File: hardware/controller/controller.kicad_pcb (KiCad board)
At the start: 4 copper layers, 53.8 x 35 mm, 82 parts, among them J1 Bus_PCI_Express_x1, J2 USB, J4 BM03B-SRSS-TB(LF)(SN), J6 RJ45_Hanrun_HR913550A_Horizon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, SW1 434133025816, SW2 434133025816, U1 RP2350A, U2 NCP1117ST33T3G, U3 W25Q128JVSIQ, U4 W6100-L, U5 RPi Radio Module 2, X1 12MHz, Y2 X322525MRB4SI

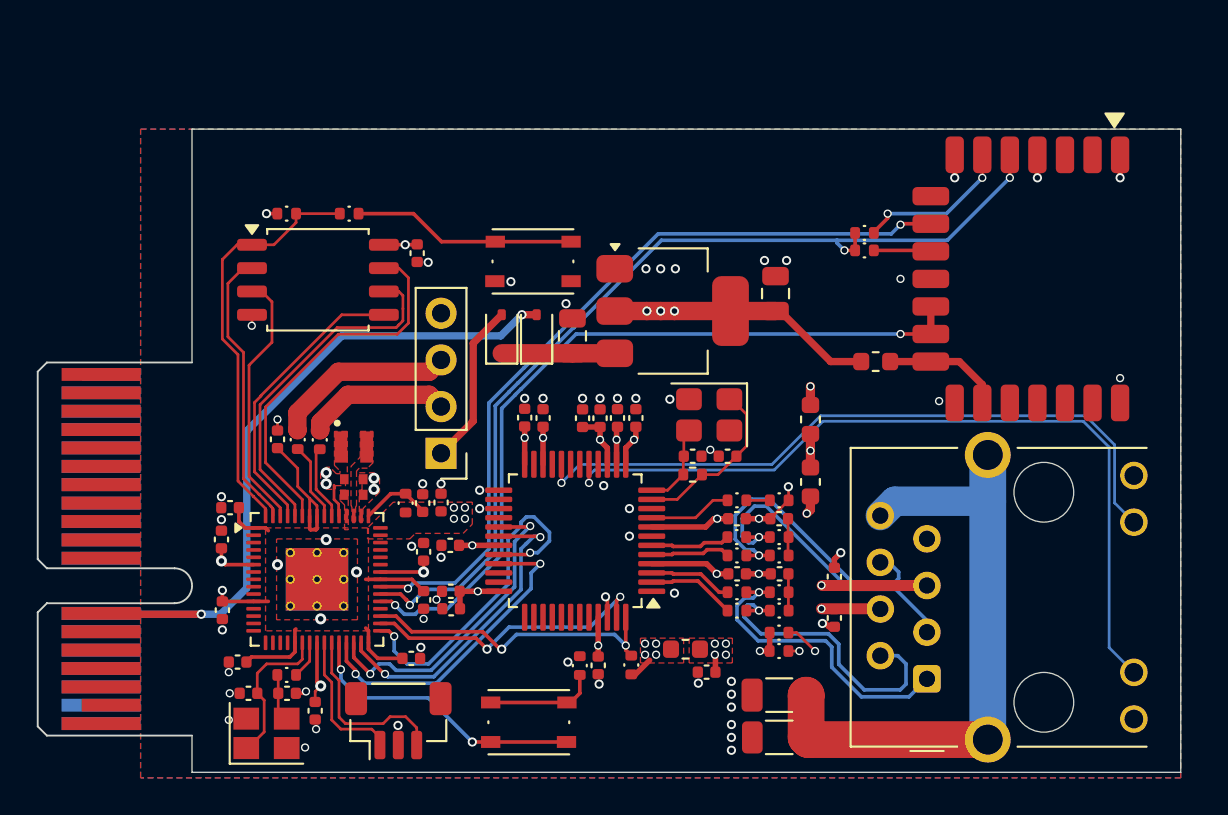
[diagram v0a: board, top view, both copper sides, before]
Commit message: feat(controller): add RPi RM2 and wire up remaining pins
fix(controller): move rj45 jack inset 1mm
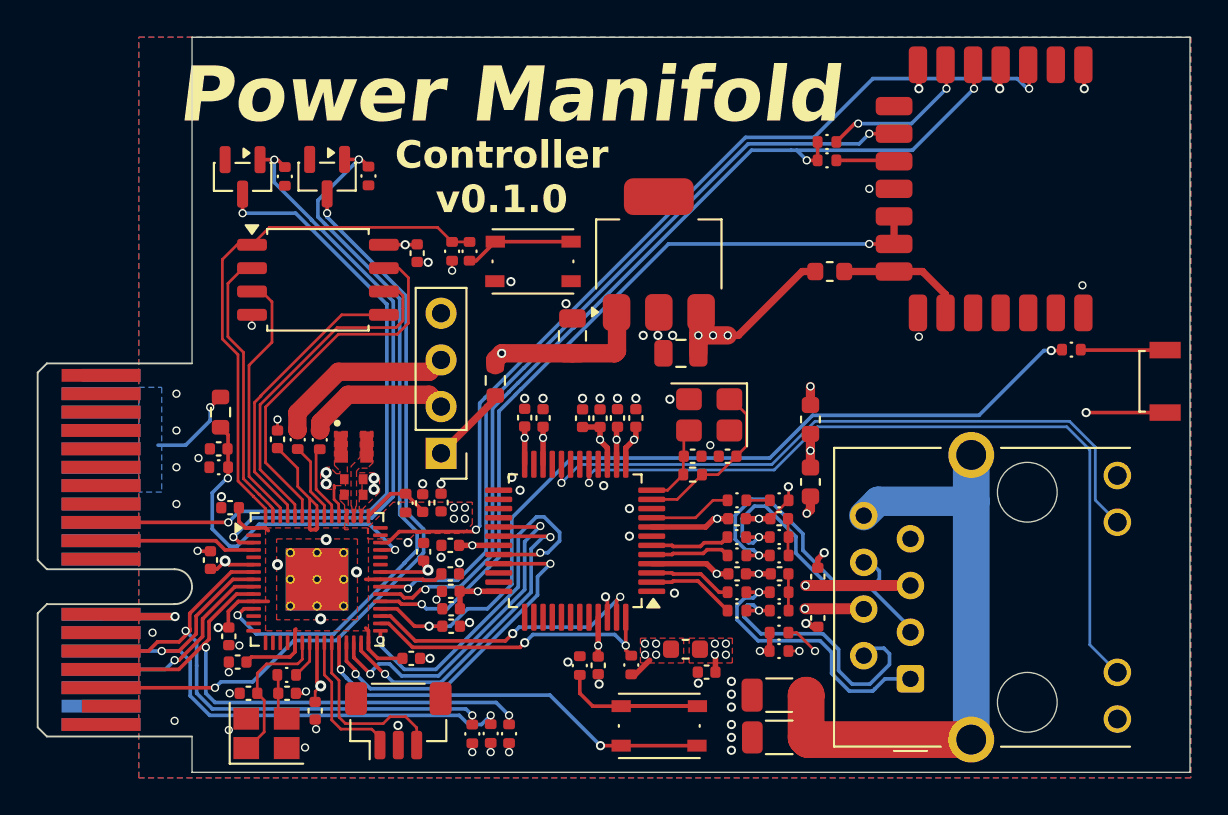
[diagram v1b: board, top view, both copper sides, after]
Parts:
- removed D1, D2: 1N5819WS, Diode_SMD:D_SOD-323
- added C18: 100nF, Capacitor_SMD:C_0402_1005Metric, F.Cu at (64.5, 57.4)
- added C27: 100nF, Capacitor_SMD:C_0402_1005Metric, F.Cu at (77.2, 67.0)
- added Q1: 2N7002, Package_TO_SOT_SMD:SOT-23, F.Cu at (65.8, 42.6)
- added Q2: 2N7002, Package_TO_SOT_SMD:SOT-23, F.Cu at (70.4, 42.6)
- added R10: 100K, Local Library:R_0402_1005Metric, F.Cu at (68.1, 42.6)
- added R11: 100K, Local Library:R_0402_1005Metric, F.Cu at (72.7, 42.5)
- added R12: 0R, Local Library:R_0603_1608Metric, F.Cu at (79.5, 53.7)
- added R13: 120K, Local Library:R_0603_1608Metric, F.Cu at (64.6, 55.4)
- added R14: 10K, Local Library:R_0402_1005Metric, F.Cu at (64.5, 58.4)
- added R15: 1K, Local Library:R_0402_1005Metric, F.Cu at (110.9, 52.0)
- added R32: 4.7K, Local Library:R_0402_1005Metric, F.Cu at (78.3, 72.9)
- added R41: 4.7K, Local Library:R_0402_1005Metric, F.Cu at (79.3, 72.9)
- added R43: 4.7K, Local Library:R_0402_1005Metric, F.Cu at (80.3, 72.9)
- added SW3: SW_Push, Button_Switch_SMD:SW_SPST_B3U-3000P, F.Cu at (116.0, 53.7)
- U2: value NCP1117ST33T3G -> AP7361C-33E; footprint Package_TO_SOT_SMD:SOT-223 -> Package_TO_SOT_SMD:SOT-223-3_TabPin2
- moved R1 9.23 mm to (77.2, 46.6), turned to 90 degrees
- moved SW2 7.10 mm to (88.5, 72.5)
- moved R6 6.86 mm to (78.2, 46.6), turned to -90 degrees
- moved C5 6.09 mm to (89.7, 52.2), turned to 180 degrees
- moved FB4 5.50 mm to (97.8, 47.8)
- moved R5 5.35 mm to (97.6, 40.7)
- moved R9 5.31 mm to (97.6, 41.7)
- moved U5 5.29 mm to (109.0, 43.2)
- moved U2 3.17 mm to (88.5, 46.8), turned to 90 degrees
- moved C13 2.03 mm to (77.1, 64.2), turned to 0 degrees
- moved C19 1.46 mm to (65.0, 67.6)
- moved C10 1.27 mm to (64.0, 63.5)
- moved C30 0.90 mm to (97.1, 64.3)
- moved C41 0.90 mm to (97.1, 66.6)
- moved J6 0.90 mm to (102.1, 69.9)
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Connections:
- J1 pad A1: Net-(J1-~{PRSNT1}) -> GND
- J1 pad A12: Net-(D2-A) -> +5V
- J1 pad A14: /SCL -> /GPIO5
- J1 pad A15: GND -> /GPIO6
- J1 pad B10: GND -> /GPIO2
- J1 pad B12: Net-(D2-A) -> +5V
- J1 pad B14: /SDA -> /GPIO4
- J1 pad B15: /~{ALERT} -> /GPIO7
- J1 pad B16: /EN -> /~{MUX_RST}
- J1 pad B17: Net-(J1-~{PRSNT1}) -> GND
- J1 pad B9: GND -> /~{EXP_RST}
- R25 pad 2: /GPIO21 -> /GPIO20
- U1 pad 3: /GPIO1 -> /EXP_RST_GATE
- U1 pad 34: /GPIO22 -> /BUTTON
- U1 pad 43: /GPIO29_ADC3 -> /GPIO29
- U2 pad 1: GND -> +5V
- U2 pad 2: +3.3V -> GND
- U2 pad 3: +5V -> +3.3V
- U4 pad 47: /GPIO20 -> /GPIO21
- U4 pad 48: /GPIO21 -> /GPIO20
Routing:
- net /GPIO29: track 0.00 -> 51.2 mm, vias 0 -> 2
- net /BUTTON: track 0.00 -> 46.6 mm, vias 0 -> 2
- net /~{MUX_RST}: track 0.00 -> 42.3 mm, vias 0 -> 2
- net Net-(D2-A): track 41.0 -> 0.00 mm, vias 2 -> 0
- net +5V: track 6.15 -> 45.7 mm, vias 0 -> 2
- net /GPIO8: track 0.00 -> 39.0 mm, vias 0 -> 2
- net /~{EXP_RST}: track 0.00 -> 37.5 mm, vias 0 -> 2
- net /EXP_RST_GATE: track 0.00 -> 33.4 mm, vias 0 -> 2
- net /GPIO5: track 0.00 -> 31.8 mm, vias 0 -> 2
- net /GPIO7: track 0.00 -> 30.9 mm, vias 0 -> 2
- net /GPIO4: track 0.00 -> 30.6 mm, vias 0 -> 2
- net /GPIO28_ADC2: track 0.00 -> 18.3 mm, vias 0 -> 2
- net /GPIO6: track 0.00 -> 10.7 mm, vias 0 -> 1
- net /GPIO2: track 0.00 -> 8.51 mm
- net /RUN: track 15.7 -> 22.7 mm
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- added copper zone on B.Cu, net /VIN
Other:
- board size 53.8 x 35 mm -> 54.3 x 40 mm

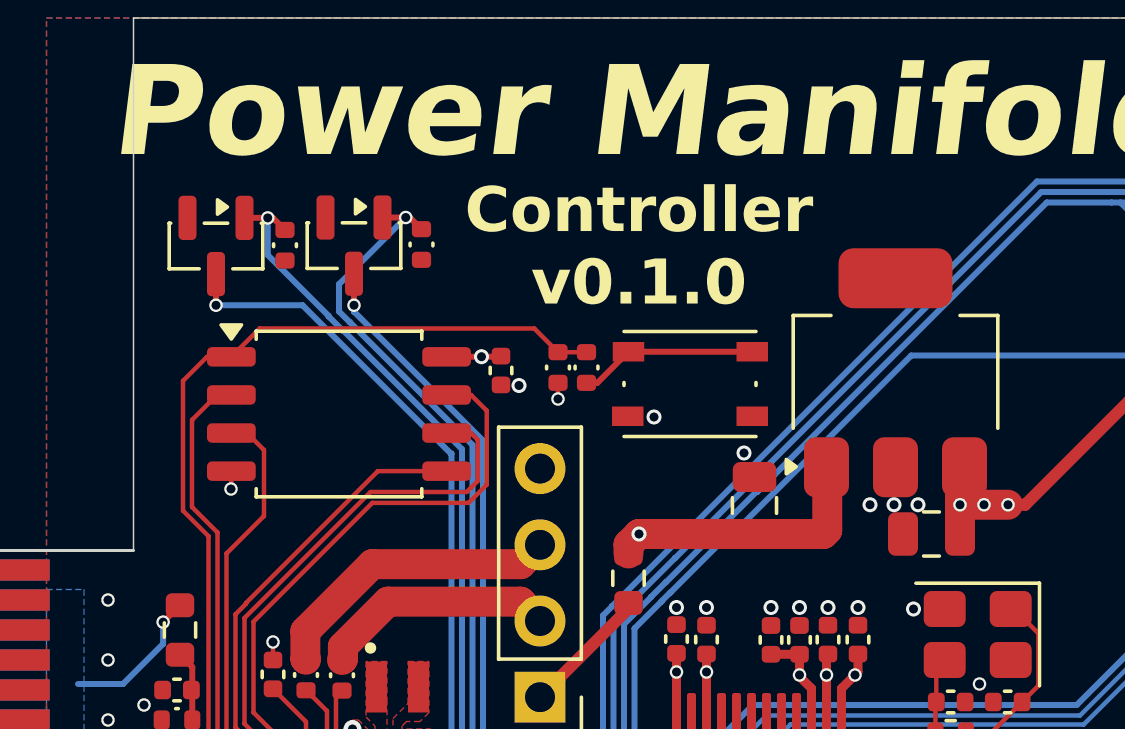
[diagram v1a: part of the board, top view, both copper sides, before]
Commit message: fix(controller): add missing ground vias
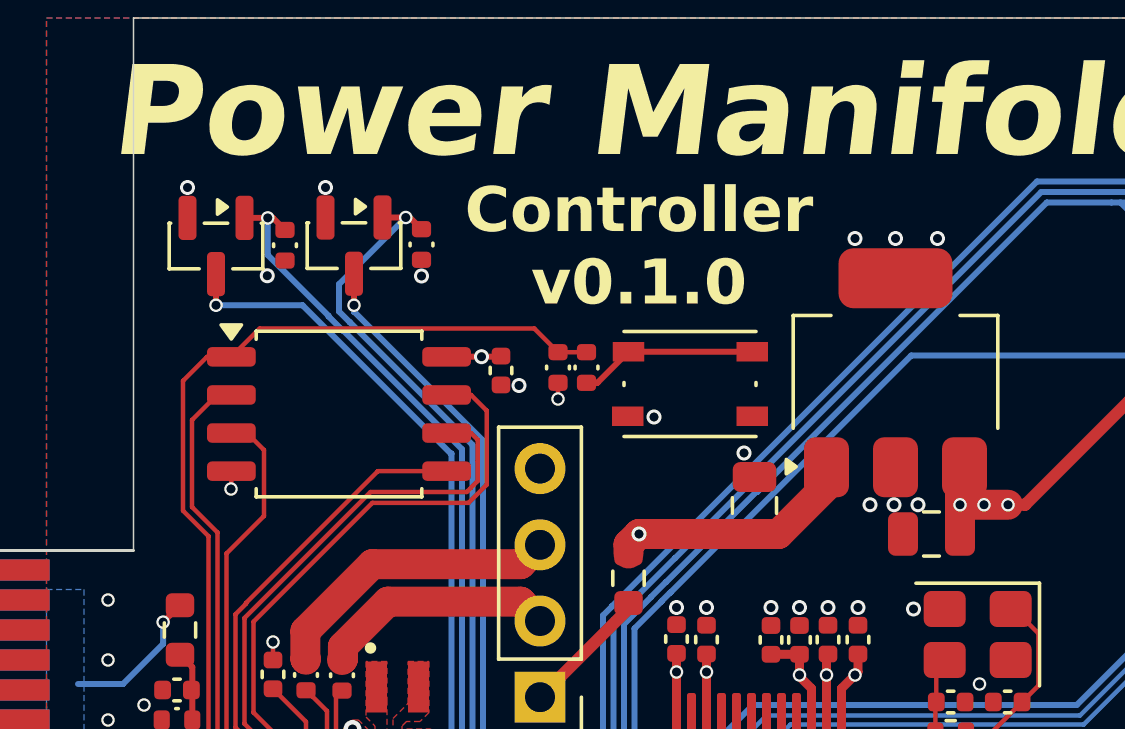
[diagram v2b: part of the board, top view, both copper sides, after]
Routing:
- net +5V: track 45.7 -> 44.8 mm
- net GND: vias 71 -> 78
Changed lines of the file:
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@@
 	)
 	(via
+		(at 89.85 42.35)
+		(size 0.5)
+		(drill 0.3)
+		(layers "F.Cu" "B.Cu")
+		(free yes)
+		(net "GND")
+	)
+	(via
 		(at 107 37.8)
 		(size 0.5)
@@
 	)
 	(via
+		(at 64.85 40.65)
+		(size 0.5)
+		(drill 0.3)
+		(layers "F.Cu" "B.Cu")
+		(free yes)
+		(net "GND")
+	)
+	(via
 		(at 99.9 43.25)
 		(size 0.45)
@@
 	)
 	(via
+		(at 67.508946 43.591054)
+		(size 0.5)
+		(drill 0.3)
+		(layers "F.Cu" "B.Cu")
+		(free yes)
+		(net "GND")
+	)
+	(via
+		(at 72.65 43.6)
+		(size 0.5)
+		(drill 0.3)
+		(layers "F.Cu" "B.Cu")
+		(free yes)
+		(net "GND")
+	)
+	(via
 		(at 75.6 59.3)
 		(size 0.5)
@@
 	)
 	(via
+		(at 87.1 42.35)
+		(size 0.5)
+		(drill 0.3)
+		(layers "F.Cu" "B.Cu")
+		(free yes)
+		(net "GND")
+	)
+	(via
 		(at 69.2 73.65)
 		(size 0.45)
@@
 	)
 	(via
+		(at 88.45 42.35)
+		(size 0.5)
+		(drill 0.3)
+		(layers "F.Cu" "B.Cu")
+		(free yes)
+		(net "GND")
+	)
+	(via
 		(at 102.6 37.8)
 		(size 0.5)
@@
 	)
 	(via
+		(at 69.45 40.65)
+		(size 0.5)
+		(drill 0.3)
+		(layers "F.Cu" "B.Cu")
+		(free yes)
+		(net "GND")
+	)
+	(via
 		(at 93.9 61.2)
 		(size 0.45)
@@
 	)
 	(segment
-		(start 86.05 52.2)
-		(end 86.175 52.075)
+		(start 86.175 50)
+		(end 86.15 49.975)
 		(width 1)
 		(layer "F.Cu")
@@
 	)
 	(segment
-		(start 86.175 50)
-		(end 86.15 49.975)
-		(width 1)
-		(layer "F.Cu")
-		(net "+5V")
-	)
-	(segment
 		(start 83.75 52.2)
-		(end 86.05 52.2)
+		(end 84.55 52.2)
 		(width 1)
 		(layer "F.Cu")
@@
 	)
 	(segment
-		(start 62.125 66.525)
-		(end 58.225184 66.525)
-		(width 0.4)
+		(start 84.55 52.2)
+		(end 86.175 50.575)
+		(width 1)
 		(layer "F.Cu")
 		(net "+5V")
 	)
 	(segment
-		(start 86.175 52.075)
+		(start 86.175 50.575)
 		(end 86.175 50)
 		(width 1)
@@
 		(net "+5V")
 	)
+	(segment
+		(start 62.125 66.525)
+		(end 58.225184 66.525)
+		(width 0.4)
+		(layer "F.Cu")
+		(net "+5V")
+	)
 	(via
 		(at 79.9 52.2)
@@
 	)
 	(segment
+		(start 111.41 52)
+		(end 111.435 52.025)
+		(width 0.2)
+		(layer "F.Cu")
+		(net "Net-(R15-Pad2)")
+	)
+	(segment
+		(start 111.435 52.025)
+		(end 116 52.025)
+		(width 0.2)
+		(layer "F.Cu")
+		(net "Net-(R15-Pad2)")
+	)
+	(segment
+		(start 74.202944 66.1)
+		(end 73.3 66.1)
+		(width 0.2)
+		(layer "F.Cu")
+		(net "/BUTTON")
+	)
+	(segment
+		(start 75.95 67.05)
+		(end 76.67 67.05)
+		(width 0.2)
+		(layer "F.Cu")
+		(net "/BUTTON")
+	)
+	(segment
+		(start 110.34 52.05)
+		(end 110.39 52)
+		(width 0.2)
+		(layer "F.Cu")
+		(net "/BUTTON")
+	)
+	(segment
+		(start 75.152944 67.05)
+		(end 74.202944 66.1)
+		(width 0.2)
+		(layer "F.Cu")
+		(net "/BUTTON")
+	)
+	(segment
+		(start 75.95 67.05)
+		(end 75.152944 67.05)
+		(width 0.2)
+		(layer "F.Cu")
+		(net "/BUTTON")
+	)
+	(segment
+		(start 109.8 52.05)
+		(end 110.34 52.05)
+		(width 0.2)
+		(layer "F.Cu")
+		(net "/BUTTON")
+	)
+	(via
+		(at 75.95 67.05)
+		(size 0.5)
+		(drill 0.3)
+		(layers "F.Cu" "B.Cu")
+		(net "/BUTTON")
+	)
+	(via
+		(at 109.8 52.05)
+		(size 0.5)
+		(drill 0.3)
+		(layers "F.Cu" "B.Cu")
+		(net "/BUTTON")
+	)
+	(segment
+		(start 105.875 55.575)
+		(end 96.815381 55.575)
+		(width 0.2)
+		(layer "B.Cu")
+		(net "/BUTTON")
+	)
+	(segment
+		(start 80.45 64.770104)
+		(end 79.120104 66.1)
+		(width 0.2)
+		(layer "B.Cu")
+		(net "/BUTTON")
+	)
+	(segment
+		(start 109.4 52.05)
+		(end 105.875 55.575)
+		(width 0.2)
+		(layer "B.Cu")
+		(net "/BUTTON")
+	)
+	(segment
+		(start 79.120104 66.1)
+		(end 78.05 66.1)
+		(width 0.2)
+		(layer "B.Cu")
+		(net "/BUTTON")
+	)
+	(segment
+		(start 96.815381 55.575)
+		(end 94.49038 57.9)
+		(width 0.2)
+		(layer "B.Cu")
+		(net "/BUTTON")
+	)
+	(segment
+		(start 80.45 61.15)
+		(end 80.45 64.770104)
+		(width 0.2)
+		(layer "B.Cu")
+		(net "/BUTTON")
+	)
+	(segment
+		(start 78.05 66.1)
+		(end 77.1 67.05)
+		(width 0.2)
+		(layer "B.Cu")
+		(net "/BUTTON")
+	)
+	(segment
+		(start 83.7 57.9)
+		(end 80.45 61.15)
+		(width 0.2)
+		(layer "B.Cu")
+		(net "/BUTTON")
+	)
+	(segment
+		(start 109.8 52.05)
+		(end 109.4 52.05)
+		(width 0.2)
+		(layer "B.Cu")
+		(net "/BUTTON")
+	)
+	(segment
+		(start 77.1 67.05)
+		(end 75.95 67.05)
+		(width 0.2)
+		(layer "B.Cu")
+		(net "/BUTTON")
+	)
+	(segment
+		(start 94.49038 57.9)
+		(end 83.7 57.9)
+		(width 0.2)
+		(layer "B.Cu")
+		(net "/BUTTON")
+	)
+	(segment
 		(start 75.75 65.05)
 		(end 75.5 65.05)
@@
 		(net "/SWD")
 	)
-	(segment
-		(start 74.202944 66.1)
-		(end 73.3 66.1)
-		(width 0.2)
-		(layer "F.Cu")
-		(net "/BUTTON")
-	)
-	(segment
-		(start 75.95 67.05)
-		(end 76.67 67.05)
-		(width 0.2)
-		(layer "F.Cu")
-		(net "/BUTTON")
-	)
-	(segment
-		(start 110.34 52.05)
-		(end 110.39 52)
-		(width 0.2)
-		(layer "F.Cu")
-		(net "/BUTTON")
-	)
-	(segment
-		(start 75.152944 67.05)
-		(end 74.202944 66.1)
-		(width 0.2)
-		(layer "F.Cu")
-		(net "/BUTTON")
-	)
-	(segment
-		(start 75.95 67.05)
-		(end 75.152944 67.05)
-		(width 0.2)
-		(layer "F.Cu")
-		(net "/BUTTON")
-	)
-	(segment
-		(start 109.8 52.05)
-		(end 110.34 52.05)
-		(width 0.2)
-		(layer "F.Cu")
-		(net "/BUTTON")
-	)
-	(via
-		(at 75.95 67.05)
-		(size 0.5)
-		(drill 0.3)
-		(layers "F.Cu" "B.Cu")
-		(net "/BUTTON")
-	)
-	(via
-		(at 109.8 52.05)
-		(size 0.5)
-		(drill 0.3)
-		(layers "F.Cu" "B.Cu")
-		(net "/BUTTON")
-	)
-	(segment
-		(start 105.875 55.575)
-		(end 96.815381 55.575)
-		(width 0.2)
-		(layer "B.Cu")
-		(net "/BUTTON")
-	)
-	(segment
-		(start 80.45 64.770104)
-		(end 79.120104 66.1)
-		(width 0.2)
-		(layer "B.Cu")
-		(net "/BUTTON")
-	)
-	(segment
-		(start 109.4 52.05)
-		(end 105.875 55.575)
-		(width 0.2)
-		(layer "B.Cu")
-		(net "/BUTTON")
-	)
-	(segment
-		(start 79.120104 66.1)
-		(end 78.05 66.1)
-		(width 0.2)
-		(layer "B.Cu")
-		(net "/BUTTON")
-	)
-	(segment
-		(start 96.815381 55.575)
-		(end 94.49038 57.9)
-		(width 0.2)
-		(layer "B.Cu")
-		(net "/BUTTON")
-	)
-	(segment
-		(start 80.45 61.15)
-		(end 80.45 64.770104)
-		(width 0.2)
-		(layer "B.Cu")
-		(net "/BUTTON")
-	)
-	(segment
-		(start 78.05 66.1)
-		(end 77.1 67.05)
-		(width 0.2)
-		(layer "B.Cu")
-		(net "/BUTTON")
-	)
-	(segment
-		(start 83.7 57.9)
-		(end 80.45 61.15)
-		(width 0.2)
-		(layer "B.Cu")
-		(net "/BUTTON")
-	)
-	(segment
-		(start 109.8 52.05)
-		(end 109.4 52.05)
-		(width 0.2)
-		(layer "B.Cu")
-		(net "/BUTTON")
-	)
-	(segment
-		(start 77.1 67.05)
-		(end 75.95 67.05)
-		(width 0.2)
-		(layer "B.Cu")
-		(net "/BUTTON")
-	)
-	(segment
-		(start 94.49038 57.9)
-		(end 83.7 57.9)
-		(width 0.2)
-		(layer "B.Cu")
-		(net "/BUTTON")
-	)
-	(segment
-		(start 111.41 52)
-		(end 111.435 52.025)
-		(width 0.2)
-		(layer "F.Cu")
-		(net "Net-(R15-Pad2)")
-	)
-	(segment
-		(start 111.435 52.025)
-		(end 116 52.025)
-		(width 0.2)
-		(layer "F.Cu")
-		(net "Net-(R15-Pad2)")
-	)
 	(zone
